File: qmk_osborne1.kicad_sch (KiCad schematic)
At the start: 2 parts

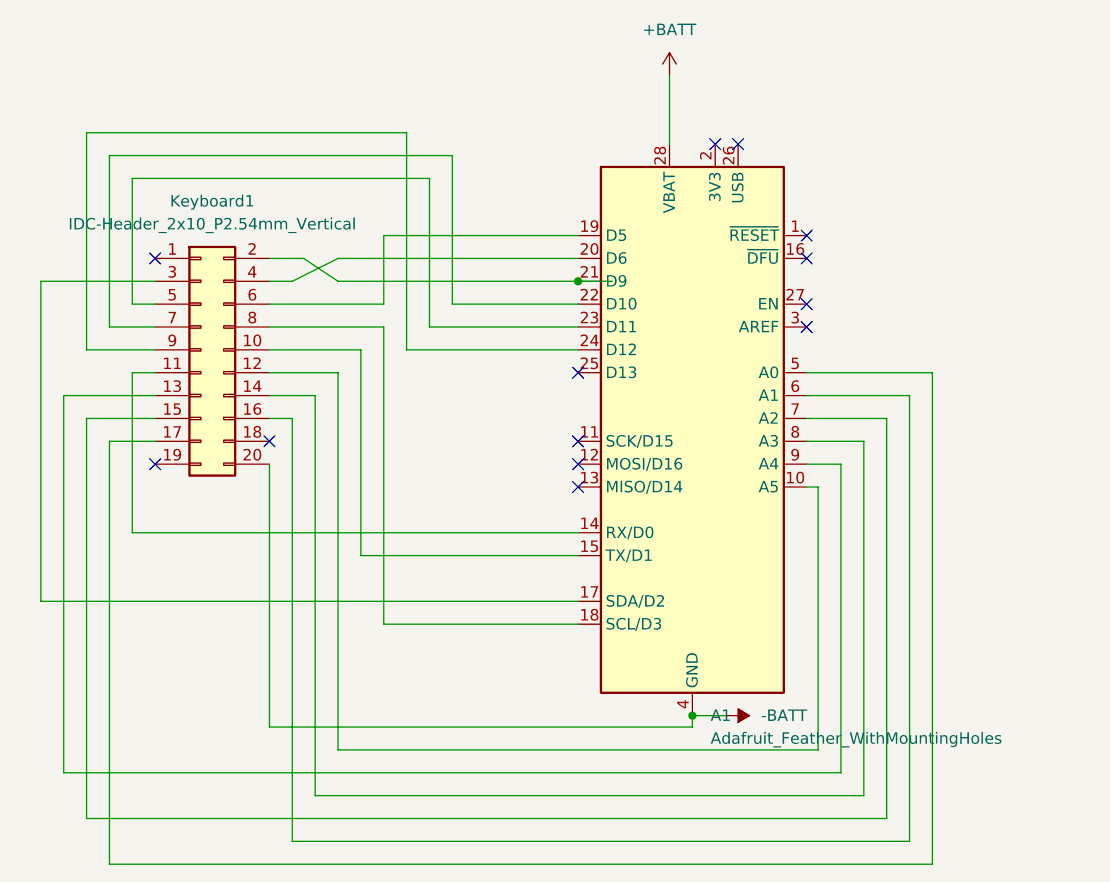
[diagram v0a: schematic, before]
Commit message: Moved row pins to be able to monitor battery voltage
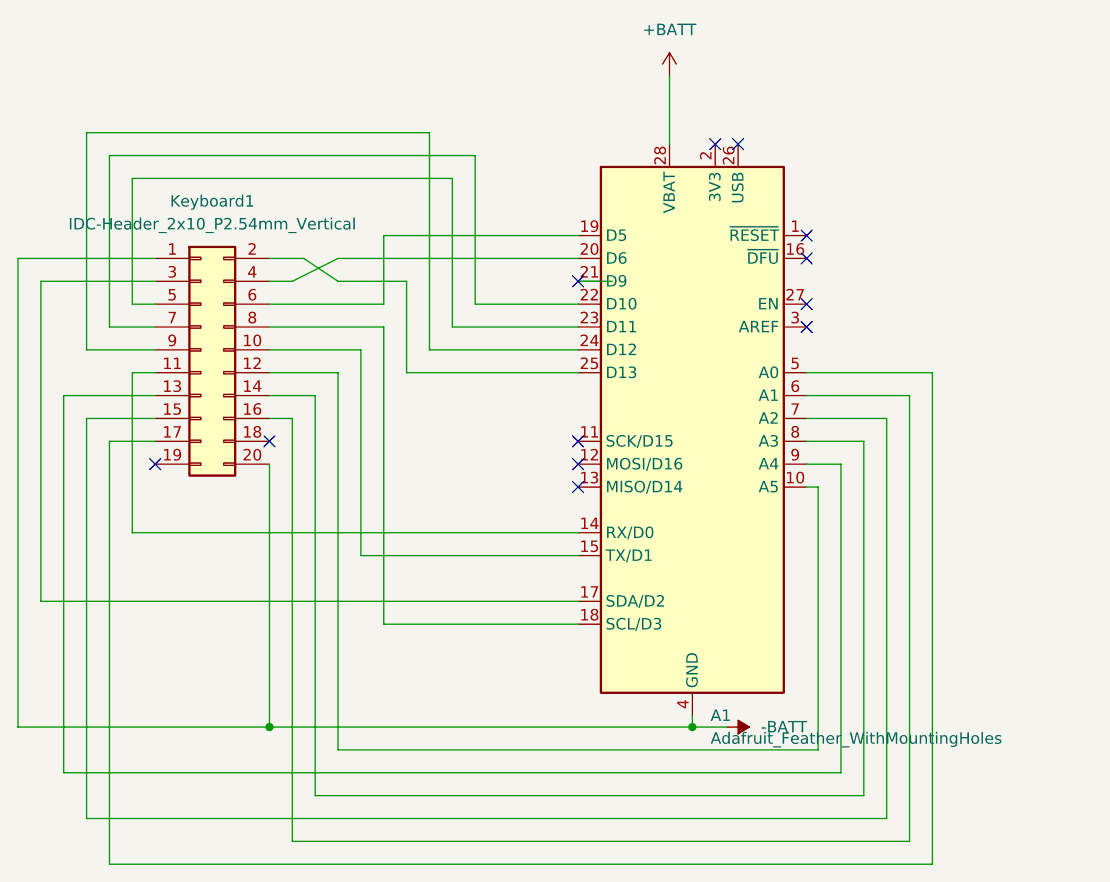
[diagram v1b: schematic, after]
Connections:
- net -BATT: now also Keyboard1.1 (Pin_1)
- net at Keyboard1.2 (Pin_2): now also A1.25 (D13); no longer A1.21 (D9)
- no-connect marks 13 -> 12
